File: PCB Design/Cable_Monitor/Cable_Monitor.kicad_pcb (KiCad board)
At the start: 2 copper layers, 63.5 x 118.1 mm, 90 parts, among them J1 USB_B_Micro, P1 type="R" model="Conn_01x32_Fe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, P2 type="R" model="Conn_01x32_Fe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, Q1 BSS316N, SW1 On / Off Button, U1 SiP32508, U2 LD1117S33TR, U3 DRV5053_THT, U4 DRV5053_THT, U5 MCP6002-xSN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

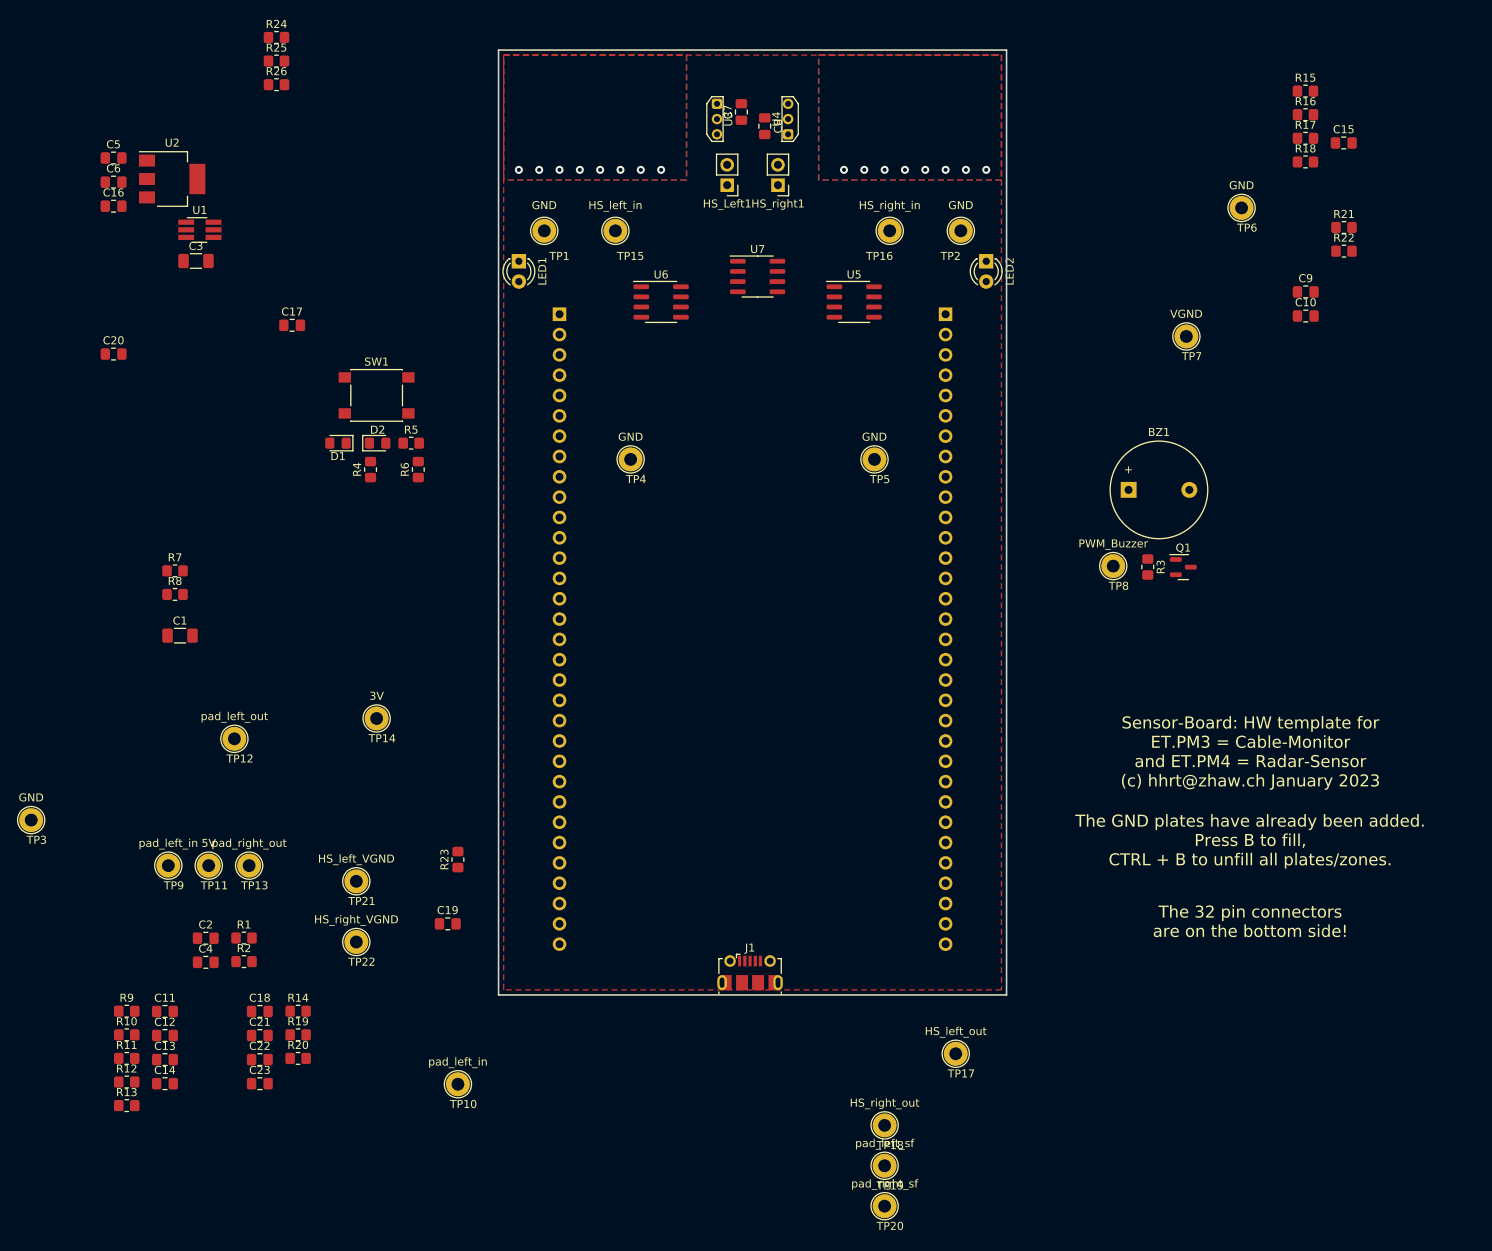
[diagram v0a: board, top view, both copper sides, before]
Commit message: Schema PDF Export
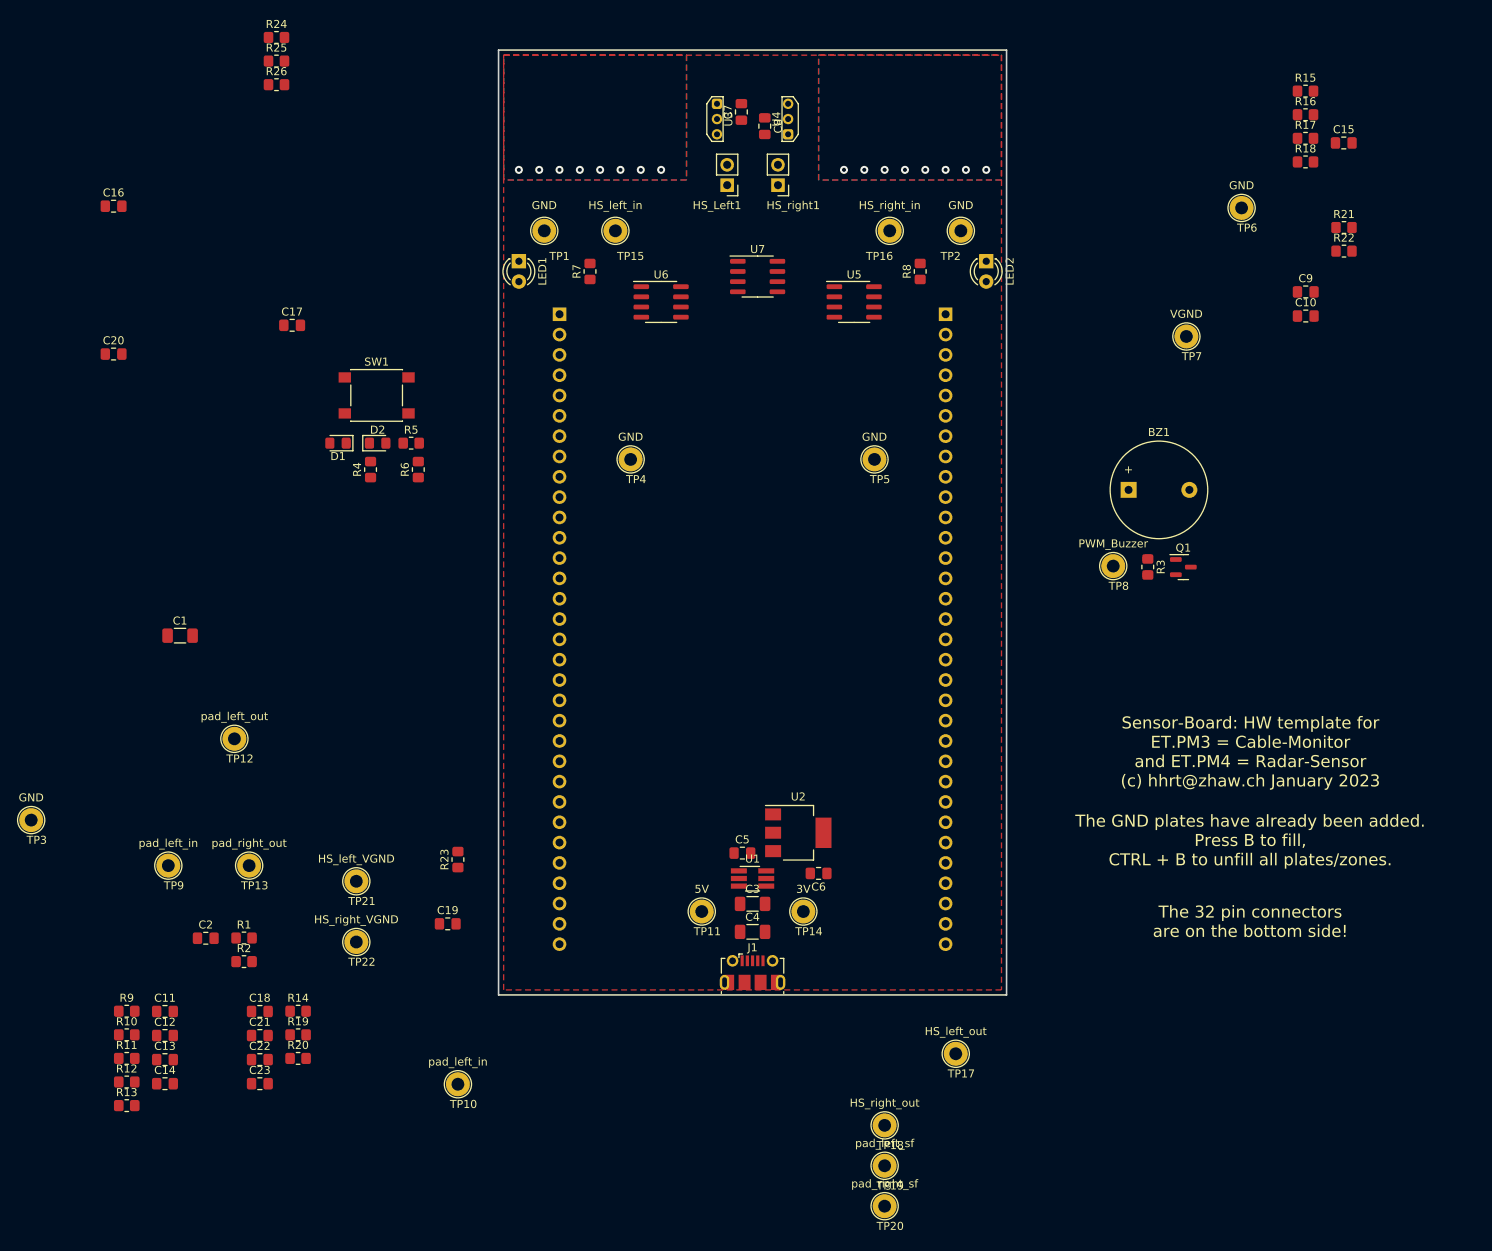
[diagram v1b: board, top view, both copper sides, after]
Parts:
- C16, C17, C22, C23: value 0.16uF -> 100nF
- C4: footprint Capacitor_SMD:C_0805_2012Metric_Pad1.18x1.45mm_HandSolder -> Capacitor_SMD:C_1206_3216Metric_Pad1.33x1.80mm_HandSolder
- R17, R18, R25, R26: value 10k -> 18k
- moved C6 123.4 mm to (144.1, 136.2), turned to 180 degrees
- moved C5 117.2 mm to (134.6, 133.7)
- moved U2 113.1 mm to (141.6, 131.1)
- moved U1 106.5 mm to (135.9, 136.8)
- moved C3 106.3 mm to (135.9, 140.0)
- moved R8 101.5 mm to (156.8, 61.0), turned to 90 degrees
- moved C4 68.5 mm to (135.9, 143.5)
- moved R7 64.0 mm to (115.6, 61.0), turned to 90 degrees
- moved TP11 61.9 mm to (129.5, 141.0)
- moved TP14 58.5 mm to (142.2, 141.0)
- moved J1 0.31 mm to (135.9, 148.6)

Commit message: Almost Donezo
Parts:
- TP10: value pad_left_in -> pad_right_in
- moved C11 128.7 mm to (156.3, 65.4), turned to 90 degrees
- moved R13 128.0 mm to (142.3, 69.2)
- moved R12 128.0 mm to (141.7, 65.8), turned to -90 degrees
- moved C12 127.2 mm to (153.1, 67.3), turned to 90 degrees
- moved R10 125.5 mm to (148.0, 69.2)
- moved TP10 119.2 mm to (146.7, 53.3)
- moved C13 116.7 mm to (131.4, 65.4), turned to 90 degrees
- moved C14 115.7 mm to (128.3, 67.3), turned to 90 degrees
- moved R11 111.0 mm to (116.8, 65.4), turned to -90 degrees
- moved C18 109.4 mm to (134.6, 62.2)
- moved R9 106.7 mm to (123.2, 69.2)
- moved TP9 102.9 mm to (125.1, 53.3)
- moved TP20 96.3 mm to (128.9, 84.5)
- moved R14 92.6 mm to (117.5, 69.2)
- moved TP22 91.2 mm to (151.1, 80.6)
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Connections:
- U6 pad 4: +3V0 -> GND
- U6 pad 8: GND -> +3V0

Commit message: Updated Schematics
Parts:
- added C24: 100nF, Capacitor_SMD:C_0805_2012Metric_Pad1.18x1.45mm_HandSolder, F.Cu at (148.8, 64.5)
- added D3: SS13L_R3G, SS13L_R3G:SODFL3618X143N, F.Cu at (129.1, 144.1)
- added D4: SS13L_R3G, SS13L_R3G:SODFL3618X143N, F.Cu at (145.4, 128.9)
- C11: value 18nF -> 100n
- C12, C14: value 330nF -> 18nF
- C13: value 18nF -> 330nF
- C15: value 100n -> 330nF
- C16: value 100nF -> 100n
- C18, C6: value 10uF -> 100nF
- C2: value 1nF -> 220nF
- C22, C7: value 100nF -> 10uF
- C5: value 100nF -> 100uF; footprint Capacitor_SMD:C_0805_2012Metric_Pad1.18x1.45mm_HandSolder -> Capacitor_SMD:C_1206_3216Metric_Pad1.33x1.80mm_HandSolder
- C9: value 100n -> 100nF
- D1, D2: value D -> SS13L_R3G; footprint Diode_SMD:D_0805_2012Metric_Pad1.15x1.40mm_HandSolder -> SS13L_R3G:SODFL3618X143N
- TP7: value VGND -> PWM_Buzzer
- TP8: value PWM_Buzzer -> VGND
- moved C22 117.3 mm to (148.8, 69.0), turned to 90 degrees
- moved C23 110.7 mm to (126.5, 64.9), turned to -90 degrees
- moved C21 110.4 mm to (143.8, 70.6), turned to 90 degrees
- moved TP3 108.9 mm to (153.7, 144.1)
- moved R19 103.3 mm to (131.6, 67.4), turned to -90 degrees
- moved TP6 103.2 mm to (148.6, 144.1)
- moved R20 102.3 mm to (133.1, 72.5), turned to 180 degrees
- moved C19 86.5 mm to (131.6, 62.9), turned to -90 degrees
- moved C7 85.0 mm to (143.8, 125.5)
- moved C1 84.4 mm to (146.8, 124.5), turned to 90 degrees
- moved R23 81.3 mm to (143.8, 66.5), turned to -90 degrees
- moved C20 81.2 mm to (137.2, 72.5), turned to 180 degrees
- moved R1 81.2 mm to (144.8, 107.7), turned to 180 degrees
- moved TP13 80.8 mm to (126.5, 74.7)
- moved R24 79.2 mm to (146.3, 69.0), turned to -90 degrees
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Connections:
- C11 pad 1: Net-(C11-Pad1) -> +3V0
- C11 pad 2: PF6 -> GND
- C12 pad 1: Net-(C11-Pad1) -> Net-(C12-Pad1)
- C12 pad 2: Net-(U5B--) -> PF6
- C13 pad 1: Net-(C13-Pad1) -> Net-(C12-Pad1)
- C13 pad 2: PC3 -> Net-(U5B--)
- C14 pad 1: Net-(C13-Pad1) -> Net-(C14-Pad1)
- C14 pad 2: Net-(U6B--) -> PC3
- C15 pad 1: +3V0 -> Net-(C14-Pad1)
- C15 pad 2: GND -> Net-(U6B--)
- C16 pad 1: GND -> +3V0
- C16 pad 2: Net-(C16-Pad2) -> GND
- C18 pad 1: Net-(C16-Pad2) -> GND
- C18 pad 2: Net-(U7A-+) -> Net-(C18-Pad2)
- C19 pad 2: Net-(U7B-+) -> Net-(U7A-+)
- C20 pad 1: Net-(C20-Pad1) -> Net-(C18-Pad2)
- C20 pad 2: GND -> Net-(U7B-+)
- C22 pad 1: PF8_ -> Net-(C22-Pad1)
- C23 pad 1: PC1_ -> PF8_
- C4 pad 1: +5V -> Enable
- C5 pad 1: Net-(U2-VI) -> +5V
- C6 pad 1: +3V0 -> Net-(U2-VI)
- C7 pad 1: GND -> Net-(D4-A)
- C7 pad 2: +3V0 -> GND
- C9 pad 1: +3V0 -> GND
- C9 pad 2: GND -> +3V0
- J1 pad 1: +5V -> Net-(D3-A)
- R11 pad 2: Net-(C13-Pad1) -> Net-(C14-Pad1)
- R12 pad 2: Net-(C11-Pad1) -> Net-(C12-Pad1)
- R13 pad 1: Net-(C11-Pad1) -> Net-(C12-Pad1)
- R14 pad 1: Net-(C13-Pad1) -> Net-(C14-Pad1)
- R17 pad 2: Net-(C16-Pad2) -> Net-(C17-Pad2)
- R18 pad 2: Net-(C17-Pad2) -> Net-(C18-Pad2)
- R22 pad 2: Net-(C20-Pad1) -> Net-(C21-Pad1)
- R24 pad 2: Net-(C21-Pad1) -> Net-(C22-Pad1)
- TP14 pad 1: +3V0 -> Net-(D4-A)
- TP7 pad 1: VGND -> PA5
- TP8 pad 1: PA5 -> VGND
- U2 pad 2: +3V0 -> Net-(D4-A)
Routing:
- net +3V0: track 0.00 -> 27.7 mm, vias 0 -> 2
- net Net-(C12-Pad1): track 0.00 -> 21.5 mm
- net pad_left: track 0.00 -> 19.4 mm
- net /hall-sensor_left_right/in_right: track 0.00 -> 14.3 mm
- net PF6: track 0.00 -> 9.95 mm, vias 0 -> 2
- net /hall-sensor_left_right/in_left: track 0.00 -> 8.36 mm
- net pad_right: track 0.00 -> 6.31 mm
- net Net-(LED1-A): track 0.00 -> 6.02 mm
- net Net-(U5A--): track 0.00 -> 4.16 mm
- net VGND: track 0.00 -> 3.34 mm
- net Net-(U5B--): track 0.00 -> 3.26 mm
- added copper zone on B.Cu, net +3V0

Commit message: Final Design Done
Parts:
- removed HS_Left1, HS_right1: Conn_01x02_Male, Connector_PinHeader_2.54mm:PinHeader_1x02_P2.54mm_Vertical
- added G***: LOGO, LOGO, F.Cu at (156.7, 41.0)
- added G***: LOGO, LOGO, F.Cu at (115.3, 40.9)
- added G***: LOGO, LOGO, B.Cu at (115.1, 41.0)
- added G***: LOGO, LOGO, B.Cu at (156.7, 41.0)
- added HS_Left: Conn_01x02_Male, Connector_PinHeader_2.54mm:PinHeader_1x02_P2.54mm_Vertical, F.Cu at (132.7, 50.2)
- added HS_right: Conn_01x02_Male, Connector_PinHeader_2.54mm:PinHeader_1x02_P2.54mm_Vertical, F.Cu at (139.1, 50.0)
- BZ1: footprint Buzzer_Beeper:Buzzer_12x9.5RM7.6 -> Buzzer_Beeper:Buzzer_D14mm_H7mm_P10mm
- J1: footprint Connector_USB:USB_Micro-B_Molex-105017-0001 -> Connector_USB:USB_Micro-B_Molex_47346-0001
- moved TP13 28.3 mm to (154.2, 68.6)
- moved TP19 14.6 mm to (128.9, 84.5)
- moved TP20 14.0 mm to (142.9, 84.5)
- moved D1 5.33 mm to (146.1, 114.0)
- moved BZ1 2.47 mm to (130.9, 94.5)
- moved D2 2.17 mm to (137.9, 114.3)
- moved C5 1.40 mm to (131.0, 130.0)
- moved TP12 1.27 mm to (117.6, 68.6)
- moved R3 0.91 mm to (135.8, 105.2)
- moved Q1 0.76 mm to (140.2, 105.0)
- moved R21 0.76 mm to (137.1, 60.7)
- moved C16 0.56 mm to (142.2, 62.4)
- moved C10 0.45 mm to (129.8, 54.1)
- moved R17 0.38 mm to (131.6, 58.2)
- moved C17 0.33 mm to (128.8, 66.3)
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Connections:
- TP14 pad 1: Net-(D4-A) -> +3V0
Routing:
- net +5V: track 0.00 -> 133.1 mm
- net VGND: track 3.34 -> 109.3 mm, vias 0 -> 4
- net PC3: track 0.00 -> 98.7 mm, vias 0 -> 2
- net PE13_: track 0.00 -> 97.0 mm, vias 0 -> 1
- net PC1_: track 0.00 -> 86.9 mm, vias 0 -> 2
- net PE15_: track 0.00 -> 63.6 mm
- net PF8_: track 0.00 -> 59.4 mm, vias 0 -> 3
- net PA5: track 0.00 -> 54.4 mm
- net PE3: track 0.00 -> 54.3 mm, vias 0 -> 1
- net Enable: track 0.00 -> 49.6 mm
- net Net-(U6A--): track 0.00 -> 47.3 mm
- net +3V0: track 27.7 -> 72.4 mm, vias 2 -> 5
- net /hall-sensor_left_right/in_right: track 14.3 -> 57.8 mm
- net Net-(U5A--): track 4.16 -> 44.8 mm
- net PE5: track 0.00 -> 40.3 mm
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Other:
- board text added: "Cable-Monitor Project for ET.PM3 ZHAW Made by A.Horvat & T.Wey 2023 V.1.0"
- board text removed: "Sensor-Board: HW template for ET.PM3 = Cable-Monitor and ET.PM4 = Radar-Sensor (c) hhrt@zhaw.ch January 2023"
- board text removed: "The 32 pin connectors are on the bottom side!"
- board text removed: "The GND plates have already been added. Press B to fill, CTRL + B to unfill all plates/zones."
